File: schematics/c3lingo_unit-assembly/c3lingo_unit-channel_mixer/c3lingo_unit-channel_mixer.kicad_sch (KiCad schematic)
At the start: 93 parts, among them J301 Interconnect, J303 I/O, Q301 MMBFJ113, SW301 OnAir_X, SW302 Mute_X, U301 TL072, U302 LM339, U303 LM339, U304 LM339, U305 LM833-N

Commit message: Refactor: Rename component rotation
The latest release of the (JLC PCB) Fabrication Toolkit plugin needs the rotation offset field to be named "FT Rotation Offset"
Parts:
- C305, C313, D314, D315, D316: FT Rotation Offset (none) -> 180; JLCPCB Rotation Offset 180 -> (none)
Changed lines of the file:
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@@
 			)
 		)
-		(property "JLCPCB Rotation Offset" ""
+		(property "FT Rotation Offset" ""
 			(at 146.05 44.45 0)
 			(effects
@@
 			)
 		)
-		(property "JLCPCB Rotation Offset" ""
+		(property "FT Rotation Offset" ""
 			(at 166.37 44.45 0)
 			(effects
@@
 			)
 		)
-		(property "JLCPCB Rotation Offset" ""
+		(property "FT Rotation Offset" ""
 			(at 156.21 40.64 0)
 			(effects
@@
 			)
 		)
-		(property "JLCPCB Rotation Offset" ""
+		(property "FT Rotation Offset" ""
 			(at 298.45 76.2 0)
 			(effects
@@
 			)
 		)
-		(property "JLCPCB Rotation Offset" ""
+		(property "FT Rotation Offset" ""
 			(at 302.26 58.42 0)
 			(effects
@@
 			)
 		)
-		(property "JLCPCB Rotation Offset" ""
+		(property "FT Rotation Offset" ""
 			(at 294.64 49.53 0)
 			(effects
@@
 			)
 		)
-		(property "JLCPCB Rotation Offset" ""
+		(property "FT Rotation Offset" ""
 			(at 274.32 72.39 0)
 			(effects
@@
 			)
 		)
-		(property "JLCPCB Rotation Offset" ""
+		(property "FT Rotation Offset" ""
 			(at 156.21 66.04 0)
 			(effects
@@
 			)
 		)
-		(property "JLCPCB Rotation Offset" ""
+		(property "FT Rotation Offset" ""
 			(at 46.99 63.5 0)
 			(effects
@@
 			)
 		)
-		(property "JLCPCB Rotation Offset" ""
+		(property "FT Rotation Offset" ""
 			(at 337.82 180.34 0)
 			(effects
@@
 			)
 		)
-		(property "JLCPCB Rotation Offset" ""
+		(property "FT Rotation Offset" ""
 			(at 321.31 180.34 0)
 			(effects
@@
 			)
 		)
-		(property "JLCPCB Rotation Offset" ""
+		(property "FT Rotation Offset" ""
 			(at 304.8 180.34 0)
 			(effects
@@
 			)
 		)
-		(property "JLCPCB Rotation Offset" ""
+		(property "FT Rotation Offset" ""
 			(at 288.29 180.34 0)
 			(effects
@@
 			)
 		)
-		(property "JLCPCB Rotation Offset" ""
+		(property "FT Rotation Offset" ""
 			(at 180.34 213.36 0)
 			(effects
@@
 			)
 		)
-		(property "JLCPCB Rotation Offset" ""
+		(property "FT Rotation Offset" ""
 			(at 271.78 180.34 0)
 			(effects
@@
 			)
 		)
-		(property "JLCPCB Rotation Offset" ""
+		(property "FT Rotation Offset" ""
 			(at 255.27 180.34 0)
 			(effects
@@
 			)
 		)
-		(property "JLCPCB Rotation Offset" ""
+		(property "FT Rotation Offset" ""
 			(at 238.76 180.34 0)
 			(effects
@@
 			)
 		)
-		(property "JLCPCB Rotation Offset" ""
+		(property "FT Rotation Offset" ""
 			(at 222.25 180.34 0)
 			(effects
@@
 			)
 		)
-		(property "JLCPCB Rotation Offset" ""
+		(property "FT Rotation Offset" ""
 			(at 205.74 180.34 0)
 			(effects
@@
 			)
 		)
-		(property "JLCPCB Rotation Offset" ""
+		(property "FT Rotation Offset" ""
 			(at 189.23 180.34 0)
 			(effects
@@
 			)
 		)
-		(property "JLCPCB Rotation Offset" ""
+		(property "FT Rotation Offset" ""
 			(at 172.72 180.34 0)
 			(effects
@@
 			)
 		)
-		(property "JLCPCB Rotation Offset" ""
+		(property "FT Rotation Offset" ""
 			(at 156.21 180.34 0)
 			(effects
@@
 			)
 		)
-		(property "JLCPCB Rotation Offset" ""
+		(property "FT Rotation Offset" ""
 			(at 337.82 156.21 0)
 			(effects
@@
 			)
 		)
-		(property "JLCPCB Rotation Offset" ""
+		(property "FT Rotation Offset" ""
 			(at 321.31 156.21 0)
 			(effects
@@
 			)
 		)
-		(property "JLCPCB Rotation Offset" ""
+		(property "FT Rotation Offset" ""
 			(at 304.8 156.21 0)
 			(effects
@@
 			)
 		)
-		(property "JLCPCB Rotation Offset" ""
+		(property "FT Rotation Offset" ""
 			(at 288.29 156.21 0)
 			(effects
@@
 			)
 		)
-		(property "JLCPCB Rotation Offset" ""
+		(property "FT Rotation Offset" ""
 			(at 271.78 156.21 0)
 			(effects
@@
 			)
 		)
-		(property "JLCPCB Rotation Offset" ""
+		(property "FT Rotation Offset" ""
 			(at 255.27 156.21 0)
 			(effects
@@
 			)
 		)
-		(property "JLCPCB Rotation Offset" ""
+		(property "FT Rotation Offset" ""
 			(at 238.76 156.21 0)
 			(effects
@@
 			)
 		)
-		(property "JLCPCB Rotation Offset" ""
+		(property "FT Rotation Offset" ""
 			(at 222.25 156.21 0)
 			(effects
@@
 			)
 		)
-		(property "JLCPCB Rotation Offset" ""
+		(property "FT Rotation Offset" ""
 			(at 205.74 156.21 0)
 			(effects
@@
 			)
 		)
-		(property "JLCPCB Rotation Offset" ""
+		(property "FT Rotation Offset" ""
 			(at 189.23 156.21 0)
 			(effects
@@
 			)
 		)
-		(property "JLCPCB Rotation Offset" ""
+		(property "FT Rotation Offset" ""
 			(at 172.72 156.21 0)
 			(effects
@@
 			)
 		)
-		(property "JLCPCB Rotation Offset" ""
+		(property "FT Rotation Offset" ""
 			(at 156.21 156.21 0)
 			(effects
@@
 			)
 		)
-		(property "JLCPCB Rotation Offset" ""
+		(property "FT Rotation Offset" ""
 			(at 246.38 213.36 0)
 			(effects
@@
 			)
 		)
-		(property "JLCPCB Rotation Offset" ""
+		(property "FT Rotation Offset" ""
 			(at 312.42 213.36 0)
 			(effects
@@
 			)
 		)
-		(property "JLCPCB Rotation Offset" ""
+		(property "FT Rotation Offset" ""
 			(at 77.47 218.44 0)
 			(effects
@@
 			)
 		)
-		(property "JLCPCB Rotation Offset" ""
+		(property "FT Rotation Offset" ""
 			(at 85.09 222.25 0)
 			(effects
@@
 			)
 		)
-		(property "JLCPCB Rotation Offset" "180"
+		(property "FT Rotation Offset" "180"
 			(at 95.25 190.5 0)
 			(effects
@@
 			)
 		)
-		(property "JLCPCB Rotation Offset" "180"
+		(property "FT Rotation Offset" "180"
 			(at 77.47 175.26 0)
 			(effects
@@
 			)
 		)
-		(property "JLCPCB Rotation Offset" ""
+		(property "FT Rotation Offset" ""
 			(at 78.74 190.5 0)
 			(effects
@@
 			)
 		)
-		(property "JLCPCB Rotation Offset" "180"
+		(property "FT Rotation Offset" "180"
 			(at 49.53 187.96 0)
 			(effects
@@
 			)
 		)
-		(property "JLCPCB Rotation Offset" ""
+		(property "FT Rotation Offset" ""
 			(at 172.72 222.25 0)
 			(effects
@@
 			)
 		)
-		(property "JLCPCB Rotation Offset" ""
+		(property "FT Rotation Offset" ""
 			(at 238.76 222.25 0)
 			(effects
@@
 			)
 		)
-		(property "JLCPCB Rotation Offset" ""
+		(property "FT Rotation Offset" ""
 			(at 304.8 222.25 0)
 			(effects
@@
 			)
 		)
-		(property "JLCPCB Rotation Offset" ""
+		(property "FT Rotation Offset" ""
 			(at 69.85 222.25 0)
 			(effects
@@
 			)
 		)
-		(property "JLCPCB Rotation Offset" ""
+		(property "FT Rotation Offset" ""
 			(at 95.25 74.93 0)
 			(effects
@@
 			)
 		)
-		(property "JLCPCB Rotation Offset" ""
+		(property "FT Rotation Offset" ""
 			(at 95.25 85.09 0)
 			(effects
@@
 			)
 		)
-		(property "JLCPCB Rotation Offset" ""
+		(property "FT Rotation Offset" ""
 			(at 66.04 66.04 0)
 			(effects
@@
 			)
 		)
-		(property "JLCPCB Rotation Offset" ""
+		(property "FT Rotation Offset" ""
 			(at 274.32 95.25 0)
 			(effects
@@
 			)
 		)
-		(property "JLCPCB Rotation Offset" ""
+		(property "FT Rotation Offset" ""
 			(at 118.11 196.85 0)
 			(effects
@@
 			)
 		)
-		(property "JLCPCB Rotation Offset" ""
+		(property "FT Rotation Offset" ""
 			(at 120.65 63.5 0)
 			(effects
@@
 			)
 		)
-		(property "JLCPCB Rotation Offset" "180"
+		(property "FT Rotation Offset" "180"
 			(at 146.05 96.52 0)
 			(effects
@@
 			)
 		)
-		(property "JLCPCB Rotation Offset" ""
+		(property "FT Rotation Offset" ""
 			(at 66.04 97.79 0)
 			(effects
@@
 			)
 		)
-		(property "JLCPCB Rotation Offset" "180"
+		(property "FT Rotation Offset" "180"
 			(at 66.04 78.74 0)
 			(effects

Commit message: Channel-Mixer: Replace mute-button connector
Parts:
- SW302: footprint Connector_PinHeader_2.54mm:PinHeader_1x02_P2.54mm_Vertical -> Connector_PinHeader_2.54mm:PinHeader_1x02_P2.54mm_Horizontal
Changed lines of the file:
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@@
 			)
 		)
-		(property "Footprint" "Connector_PinHeader_2.54mm:PinHeader_1x02_P2.54mm_Vertical"
+		(property "Footprint" "Connector_PinHeader_2.54mm:PinHeader_1x02_P2.54mm_Horizontal"
 			(at 104.14 99.06 0)
 			(effects

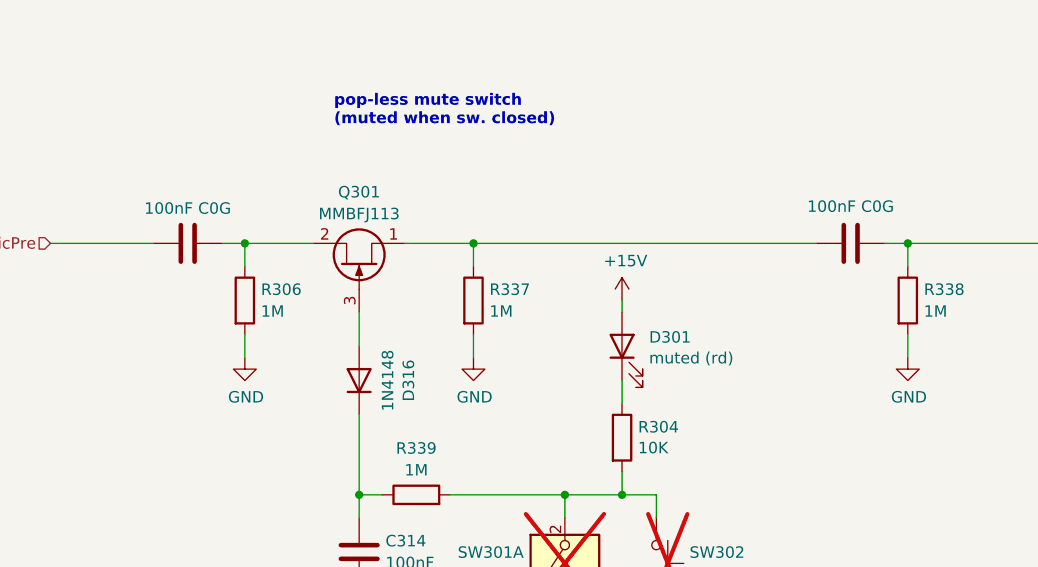
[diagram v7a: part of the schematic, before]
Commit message: Channel-Mixer: Change mute LED to 3mm THD
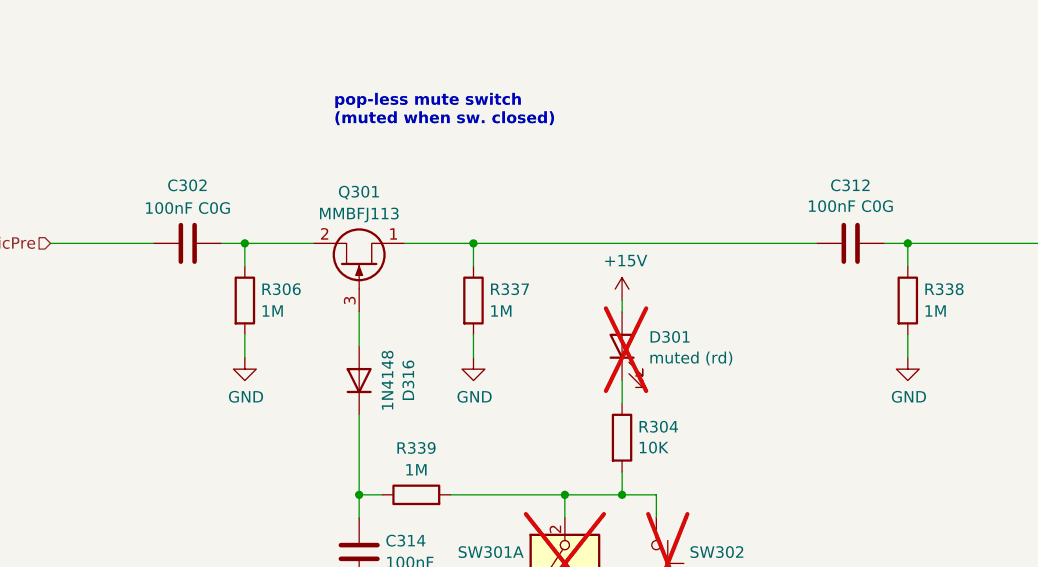
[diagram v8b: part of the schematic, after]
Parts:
- D301: footprint LED_SMD:LED_0805_2012Metric_Pad1.15x1.40mm_HandSolder -> LED_THT:LED_D3.0mm; LCSC Part # C84256 -> (none); Model generic 20 mA, 2.0 V -> Kingbright WP710A10LID; now not fitted
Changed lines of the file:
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@@
 	(title_block
 		(title "c3lingo interpeter unit -- channel mixer")
-		(date "2025-08-26")
-		(rev "v0.4.0")
+		(date "2025-09-19")
+		(rev "v0.5.0-dev")
 		(company "Jannik Beyerstedt (jtbx)")
-		(comment 1 "Prototype 3")
+		(comment 1 "Prototype 3b")
 	)
 	(text "Summing Module\nGain: -inf to 0 dB per Ch."
@@
 					(size 1.27 1.27)
 				)
-				(hide yes)
 			)
 		)
@@
 		(in_bom yes)
 		(on_board yes)
-		(dnp no)
+		(dnp yes)
 		(property "Reference" "D301"
 			(at 98.2472 73.9394 90)
@@
 			)
 		)
-		(property "Footprint" "LED_SMD:LED_0805_2012Metric_Pad1.15x1.40mm_HandSolder"
+		(property "Footprint" "LED_THT:LED_D3.0mm"
 			(at 95.25 74.93 0)
 			(effects
@@
 			)
 		)
-		(property "Model" "generic 20 mA, 2.0 V"
+		(property "Model" "Kingbright WP710A10LID"
 			(at 95.25 74.93 0)
 			(effects
@@
 			)
 		)
-		(property "LCSC Part #" "C84256"
+		(property "LCSC Part #" ""
 			(at 95.25 74.93 0)
 			(effects
@@
 					(size 1.27 1.27)
 				)
-				(hide yes)
 			)
 		)
